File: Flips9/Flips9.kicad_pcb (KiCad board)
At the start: 2 copper layers, 100 x 100 mm, 44 parts, among them CN1 UFP2810, U1 74238, U11 74238, U12 74238, U13 TD62783, U14 ULN2803/2003, U21 74238, U22 74238, U23 TD62783, U24 ULN2803/2003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

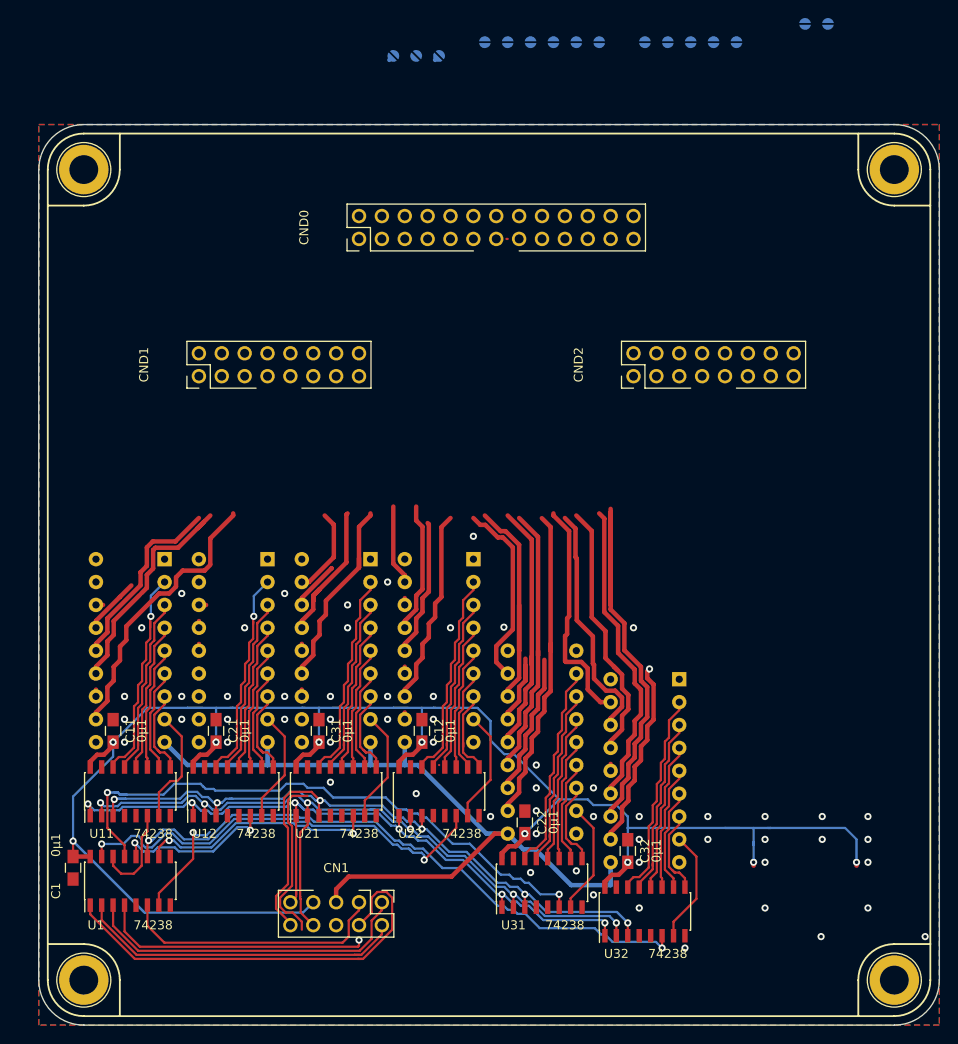
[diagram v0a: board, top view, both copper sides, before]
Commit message: prepare traces of flips9
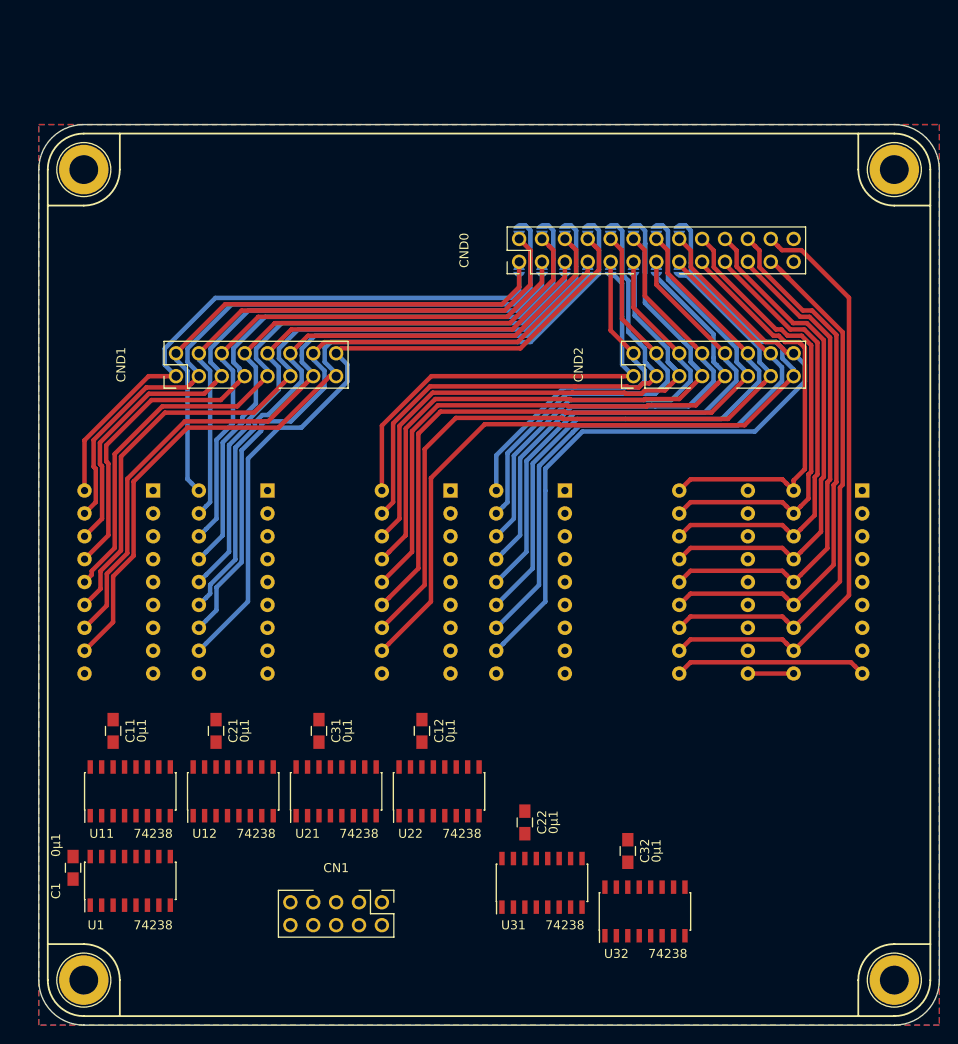
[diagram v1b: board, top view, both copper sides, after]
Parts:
- moved JP115 30.8 mm to (121.9, 67.1), turned to 90 degrees
- moved U34 29.2 mm to (142.2, 91.4)
- moved JP116 28.2 mm to (121.9, 62.5)
- moved JP111 27.9 mm to (116.8, 67.1)
- moved JP101 27.7 mm to (104.1, 67.1), turned to 90 degrees
- moved JP103 26.5 mm to (106.7, 67.1), turned to 90 degrees
- moved JP109 26.2 mm to (114.3, 67.1)
- moved JP113 26.2 mm to (119.4, 67.1)
- moved U33 26.1 mm to (129.5, 91.4)
- moved JP105 25.7 mm to (109.2, 67.1)
- moved JP107 25.7 mm to (111.8, 67.1)
- moved JP110 22.6 mm to (114.3, 62.5), turned to 270 degrees
- moved JP114 22.6 mm to (119.4, 62.5), turned to 270 degrees
- moved JP102 22.4 mm to (104.1, 62.5), turned to 270 degrees
- moved JP104 21.8 mm to (106.7, 62.5), turned to 270 degrees
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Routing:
- net VCC: track 211.6 -> 0.00 mm, vias 9 -> 0
- net /UnitY/A2: track 96.3 -> 0.00 mm, vias 6 -> 0
- net /SX16: track 0.00 -> 89.8 mm
- net /UnitY/A1: track 87.9 -> 0.00 mm, vias 6 -> 0
- net /UnitY/A0: track 84.3 -> 0.00 mm, vias 6 -> 0
- net +24V: track 89.3 -> 5.08 mm
- net /SX7: track 0.76 -> 82.6 mm
- net /SX15: track 0.76 -> 79.6 mm
- net /Y8: track 0.00 -> 78.8 mm
- net /Y16: track 0.76 -> 78.0 mm
- net /SX2: track 0.00 -> 75.8 mm
- net /SX4: track 6.33 -> 81.9 mm
- net /Y7: track 0.00 -> 73.8 mm
- net /Y6: track 0.00 -> 73.4 mm
- net /SX3: track 0.91 -> 72.3 mm
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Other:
- board text removed: "8"
- board text removed: "U34 = ULN2803"

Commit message: Rotate connectors CN1,2
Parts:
- moved CND2 18.0 mm to (134.6, 76.2), turned to 270 degrees
- moved CND1 18.0 mm to (83.8, 76.2), turned to 270 degrees
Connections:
- CND1 pad 1: /SX1 -> /Y8
- CND1 pad 10: /Y5 -> /SX4
- CND1 pad 11: /SX6 -> /Y3
- CND1 pad 12: /Y6 -> /SX3
- CND1 pad 13: /SX7 -> /Y2
- CND1 pad 14: /Y7 -> /SX2
- CND1 pad 15: /SX8 -> /Y1
- CND1 pad 16: /Y8 -> /SX1
- CND1 pad 2: /Y1 -> /SX8
- CND1 pad 3: /SX2 -> /Y7
- CND1 pad 4: /Y2 -> /SX7
- CND1 pad 5: /SX3 -> /Y6
- CND1 pad 6: /Y3 -> /SX6
- CND1 pad 7: /SX4 -> /Y5
- CND1 pad 8: /Y4 -> /SX5
- CND1 pad 9: /SX5 -> /Y4
- CND2 pad 1: /SX9 -> /Y16
- CND2 pad 10: /Y13 -> /SX12
- CND2 pad 11: /SX14 -> /Y11
- CND2 pad 12: /Y14 -> /SX11
- CND2 pad 13: /SX15 -> /Y10
- CND2 pad 14: /Y15 -> /SX10
- CND2 pad 15: /SX16 -> /Y9
- CND2 pad 16: /Y16 -> /SX9
- CND2 pad 2: /Y9 -> /SX16
- CND2 pad 3: /SX10 -> /Y15
- CND2 pad 4: /Y10 -> /SX15
- CND2 pad 5: /SX11 -> /Y14
- CND2 pad 6: /Y11 -> /SX14
- CND2 pad 7: /SX12 -> /Y13
- CND2 pad 8: /Y12 -> /SX13
- CND2 pad 9: /SX13 -> /Y12
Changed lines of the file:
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@@
   (page A4)
   (layers
-    (0 F.Cu signal hide)
+    (0 F.Cu signal)
     (31 B.Cu signal)
     (36 B.SilkS user)
@@
   )
   (module Own:Pin_Header_Straight_Shrouded_Locks_2x08_Pitch2.54mm_ConvNumbering (layer F.Cu)
-    (at 66.04 78.74 90)
+    (at 83.82 76.2 270)
     (descr "Through hole shrouded straight pin header with locks, 2x08, 2.54mm pitch, double rows, conventional numbering")
     (tags "Through hole shrouded straight pin header with locks THT 2x08 2.54mm double row, conventional numbering")
-    (fp_text reference CND1 (at 1.27 -6.096 90) (layer F.SilkS)
-      (effects (font (size 1 1) (thickness 0.15)))
-    )
-    (fp_text value Conn_02x08_Odd_Even (at 4.826 5.08 180) (layer F.Fab) hide
-      (effects (font (size 1 1) (thickness 0.15)))
-    )
-    (fp_text user %R (at 1.27 5.08 180) (layer F.Fab)
+    (fp_text reference CND1 (at 1.27 -6.096 270) (layer F.SilkS)
+      (effects (font (size 1 1) (thickness 0.15)))
+    )
+    (fp_text value Conn_02x08_Odd_Even (at 4.826 5.08) (layer F.Fab) hide
+      (effects (font (size 1 1) (thickness 0.15)))
+    )
+    (fp_text user %R (at 1.27 5.08) (layer F.Fab)
       (effects (font (size 1 1) (thickness 0.15)))
     )
@@
     (fp_line (start -3.33 28.9) (end 5.87 28.9) (layer F.CrtYd) (width 0.05))
     (fp_line (start 5.87 28.9) (end 5.87 -11.12) (layer F.CrtYd) (width 0.05))
-    (pad 1 thru_hole oval (at 0 0 90) (size 1.6 1.6) (drill 1) (layers *.Cu *.Mask)
+    (pad 1 thru_hole oval (at 0 0 270) (size 1.6 1.6) (drill 1) (layers *.Cu *.Mask)
+      (net 74 /Y8))
+    (pad 2 thru_hole oval (at 2.54 0 270) (size 1.6 1.6) (drill 1) (layers *.Cu *.Mask)
+      (net 100 /SX8))
+    (pad 3 thru_hole oval (at 0 2.54 270) (size 1.6 1.6) (drill 1) (layers *.Cu *.Mask)
+      (net 73 /Y7))
+    (pad 4 thru_hole oval (at 2.54 2.54 270) (size 1.6 1.6) (drill 1) (layers *.Cu *.Mask)
+      (net 99 /SX7))
+    (pad 5 thru_hole oval (at 0 5.08 270) (size 1.6 1.6) (drill 1) (layers *.Cu *.Mask)
+      (net 72 /Y6))
+    (pad 6 thru_hole oval (at 2.54 5.08 270) (size 1.6 1.6) (drill 1) (layers *.Cu *.Mask)
+      (net 98 /SX6))
+    (pad 7 thru_hole oval (at 0 7.62 270) (size 1.6 1.6) (drill 1) (layers *.Cu *.Mask)
+      (net 71 /Y5))
+    (pad 8 thru_hole oval (at 2.54 7.62 270) (size 1.6 1.6) (drill 1) (layers *.Cu *.Mask)
+      (net 97 /SX5))
+    (pad 9 thru_hole oval (at 0 10.16 270) (size 1.6 1.6) (drill 1) (layers *.Cu *.Mask)
+      (net 70 /Y4))
+    (pad 10 thru_hole oval (at 2.54 10.16 270) (size 1.6 1.6) (drill 1) (layers *.Cu *.Mask)
+      (net 96 /SX4))
+    (pad 11 thru_hole oval (at 0 12.7 270) (size 1.6 1.6) (drill 1) (layers *.Cu *.Mask)
+      (net 69 /Y3))
+    (pad 12 thru_hole oval (at 2.54 12.7 270) (size 1.6 1.6) (drill 1) (layers *.Cu *.Mask)
+      (net 95 /SX3))
+    (pad 13 thru_hole oval (at 0 15.24 270) (size 1.6 1.6) (drill 1) (layers *.Cu *.Mask)
+      (net 68 /Y2))
+    (pad 14 thru_hole oval (at 2.54 15.24 270) (size 1.6 1.6) (drill 1) (layers *.Cu *.Mask)
+      (net 94 /SX2))
+    (pad 15 thru_hole oval (at 0 17.78 270) (size 1.6 1.6) (drill 1) (layers *.Cu *.Mask)
+      (net 67 /Y1))
+    (pad 16 thru_hole oval (at 2.54 17.78 270) (size 1.6 1.6) (drill 1) (layers *.Cu *.Mask)
       (net 93 /SX1))
-    (pad 2 thru_hole oval (at 2.54 0 90) (size 1.6 1.6) (drill 1) (layers *.Cu *.Mask)
-      (net 67 /Y1))
-    (pad 3 thru_hole oval (at 0 2.54 90) (size 1.6 1.6) (drill 1) (layers *.Cu *.Mask)
-      (net 94 /SX2))
-    (pad 4 thru_hole oval (at 2.54 2.54 90) (size 1.6 1.6) (drill 1) (layers *.Cu *.Mask)
-      (net 68 /Y2))
-    (pad 5 thru_hole oval (at 0 5.08 90) (size 1.6 1.6) (drill 1) (layers *.Cu *.Mask)
-      (net 95 /SX3))
-    (pad 6 thru_hole oval (at 2.54 5.08 90) (size 1.6 1.6) (drill 1) (layers *.Cu *.Mask)
-      (net 69 /Y3))
-    (pad 7 thru_hole oval (at 0 7.62 90) (size 1.6 1.6) (drill 1) (layers *.Cu *.Mask)
-      (net 96 /SX4))
-    (pad 8 thru_hole oval (at 2.54 7.62 90) (size 1.6 1.6) (drill 1) (layers *.Cu *.Mask)
-      (net 70 /Y4))
-    (pad 9 thru_hole oval (at 0 10.16 90) (size 1.6 1.6) (drill 1) (layers *.Cu *.Mask)
-      (net 97 /SX5))
-    (pad 10 thru_hole oval (at 2.54 10.16 90) (size 1.6 1.6) (drill 1) (layers *.Cu *.Mask)
-      (net 71 /Y5))
-    (pad 11 thru_hole oval (at 0 12.7 90) (size 1.6 1.6) (drill 1) (layers *.Cu *.Mask)
-      (net 98 /SX6))
-    (pad 12 thru_hole oval (at 2.54 12.7 90) (size 1.6 1.6) (drill 1) (layers *.Cu *.Mask)
-      (net 72 /Y6))
-    (pad 13 thru_hole oval (at 0 15.24 90) (size 1.6 1.6) (drill 1) (layers *.Cu *.Mask)
-      (net 99 /SX7))
-    (pad 14 thru_hole oval (at 2.54 15.24 90) (size 1.6 1.6) (drill 1) (layers *.Cu *.Mask)
-      (net 73 /Y7))
-    (pad 15 thru_hole oval (at 0 17.78 90) (size 1.6 1.6) (drill 1) (layers *.Cu *.Mask)
-      (net 100 /SX8))
-    (pad 16 thru_hole oval (at 2.54 17.78 90) (size 1.6 1.6) (drill 1) (layers *.Cu *.Mask)
-      (net 74 /Y8))
     (model ${KISYS3DMOD}/Connector_IDC.3dshapes/IDC-Header_2x08_P2.54mm_Vertical.step
       (at (xyz 0 0 0))
@@
   )
   (module Own:Pin_Header_Straight_Shrouded_Locks_2x08_Pitch2.54mm_ConvNumbering (layer F.Cu)
-    (at 116.84 78.74 90)
+    (at 134.62 76.2 270)
     (descr "Through hole shrouded straight pin header with locks, 2x08, 2.54mm pitch, double rows, conventional numbering")
     (tags "Through hole shrouded straight pin header with locks THT 2x08 2.54mm double row, conventional numbering")
-    (fp_text reference CND2 (at 1.27 -6.096 90) (layer F.SilkS)
-      (effects (font (size 1 1) (thickness 0.15)))
-    )
-    (fp_text value Conn_02x08_Odd_Even (at 4.826 5.08 180) (layer F.Fab) hide
+    (fp_text reference CND2 (at 1.27 -6.096 270) (layer F.SilkS)
+      (effects (font (size 1 1) (thickness 0.15)))
+    )
+    (fp_text value Conn_02x08_Odd_Even (at 4.826 5.08) (layer F.Fab) hide
       (effects (font (size 1 1) (thickness 0.15)))
     )
@@
     (fp_line (start -1.33 0) (end -1.33 -1.33) (layer F.SilkS) (width 0.12))
     (fp_line (start -1.33 -1.33) (end 0 -1.33) (layer F.SilkS) (width 0.12))
-    (fp_text user %R (at 1.27 5.08 180) (layer F.Fab)
-      (effects (font (size 1 1) (thickness 0.15)))
-    )
-    (pad 16 thru_hole oval (at 2.54 17.78 90) (size 1.6 1.6) (drill 1) (layers *.Cu *.Mask)
+    (fp_text user %R (at 1.27 5.08) (layer F.Fab)
+      (effects (font (size 1 1) (thickness 0.15)))
+    )
+    (pad 16 thru_hole oval (at 2.54 17.78 270) (size 1.6 1.6) (drill 1) (layers *.Cu *.Mask)
+      (net 108 /SX9))
+    (pad 15 thru_hole oval (at 0 17.78 270) (size 1.6 1.6) (drill 1) (layers *.Cu *.Mask)
+      (net 75 /Y9))
+    (pad 14 thru_hole oval (at 2.54 15.24 270) (size 1.6 1.6) (drill 1) (layers *.Cu *.Mask)
+      (net 107 /SX10))
+    (pad 13 thru_hole oval (at 0 15.24 270) (size 1.6 1.6) (drill 1) (layers *.Cu *.Mask)
+      (net 76 /Y10))
+    (pad 12 thru_hole oval (at 2.54 12.7 270) (size 1.6 1.6) (drill 1) (layers *.Cu *.Mask)
+      (net 106 /SX11))
+    (pad 11 thru_hole oval (at 0 12.7 270) (size 1.6 1.6) (drill 1) (layers *.Cu *.Mask)
+      (net 77 /Y11))
+    (pad 10 thru_hole oval (at 2.54 10.16 270) (size 1.6 1.6) (drill 1) (layers *.Cu *.Mask)
+      (net 105 /SX12))
+    (pad 9 thru_hole oval (at 0 10.16 270) (size 1.6 1.6) (drill 1) (layers *.Cu *.Mask)
+      (net 78 /Y12))
+    (pad 8 thru_hole oval (at 2.54 7.62 270) (size 1.6 1.6) (drill 1) (layers *.Cu *.Mask)
+      (net 104 /SX13))
+    (pad 7 thru_hole oval (at 0 7.62 270) (size 1.6 1.6) (drill 1) (layers *.Cu *.Mask)
+      (net 79 /Y13))
+    (pad 6 thru_hole oval (at 2.54 5.08 270) (size 1.6 1.6) (drill 1) (layers *.Cu *.Mask)
+      (net 103 /SX14))
+    (pad 5 thru_hole oval (at 0 5.08 270) (size 1.6 1.6) (drill 1) (layers *.Cu *.Mask)
+      (net 80 /Y14))
+    (pad 4 thru_hole oval (at 2.54 2.54 270) (size 1.6 1.6) (drill 1) (layers *.Cu *.Mask)
+      (net 102 /SX15))
+    (pad 3 thru_hole oval (at 0 2.54 270) (size 1.6 1.6) (drill 1) (layers *.Cu *.Mask)
+      (net 81 /Y15))
+    (pad 2 thru_hole oval (at 2.54 0 270) (size 1.6 1.6) (drill 1) (layers *.Cu *.Mask)
+      (net 101 /SX16))
+    (pad 1 thru_hole oval (at 0 0 270) (size 1.6 1.6) (drill 1) (layers *.Cu *.Mask)
       (net 82 /Y16))
-    (pad 15 thru_hole oval (at 0 17.78 90) (size 1.6 1.6) (drill 1) (layers *.Cu *.Mask)
-      (net 101 /SX16))
-    (pad 14 thru_hole oval (at 2.54 15.24 90) (size 1.6 1.6) (drill 1) (layers *.Cu *.Mask)
-      (net 81 /Y15))
-    (pad 13 thru_hole oval (at 0 15.24 90) (size 1.6 1.6) (drill 1) (layers *.Cu *.Mask)
-      (net 102 /SX15))
-    (pad 12 thru_hole oval (at 2.54 12.7 90) (size 1.6 1.6) (drill 1) (layers *.Cu *.Mask)
-      (net 80 /Y14))
-    (pad 11 thru_hole oval (at 0 12.7 90) (size 1.6 1.6) (drill 1) (layers *.Cu *.Mask)
-      (net 103 /SX14))
-    (pad 10 thru_hole oval (at 2.54 10.16 90) (size 1.6 1.6) (drill 1) (layers *.Cu *.Mask)
-      (net 79 /Y13))
-    (pad 9 thru_hole oval (at 0 10.16 90) (size 1.6 1.6) (drill 1) (layers *.Cu *.Mask)
-      (net 104 /SX13))
-    (pad 8 thru_hole oval (at 2.54 7.62 90) (size 1.6 1.6) (drill 1) (layers *.Cu *.Mask)
-      (net 78 /Y12))
-    (pad 7 thru_hole oval (at 0 7.62 90) (size 1.6 1.6) (drill 1) (layers *.Cu *.Mask)
-      (net 105 /SX12))
-    (pad 6 thru_hole oval (at 2.54 5.08 90) (size 1.6 1.6) (drill 1) (layers *.Cu *.Mask)
-      (net 77 /Y11))
-    (pad 5 thru_hole oval (at 0 5.08 90) (size 1.6 1.6) (drill 1) (layers *.Cu *.Mask)
-      (net 106 /SX11))
-    (pad 4 thru_hole oval (at 2.54 2.54 90) (size 1.6 1.6) (drill 1) (layers *.Cu *.Mask)
-      (net 76 /Y10))
-    (pad 3 thru_hole oval (at 0 2.54 90) (size 1.6 1.6) (drill 1) (layers *.Cu *.Mask)
-      (net 107 /SX10))
-    (pad 2 thru_hole oval (at 2.54 0 90) (size 1.6 1.6) (drill 1) (layers *.Cu *.Mask)
-      (net 75 /Y9))
-    (pad 1 thru_hole oval (at 0 0 90) (size 1.6 1.6) (drill 1) (layers *.Cu *.Mask)
-      (net 108 /SX9))
     (model ${KISYS3DMOD}/Connector_IDC.3dshapes/IDC-Header_2x08_P2.54mm_Vertical.step
       (at (xyz 0 0 0))

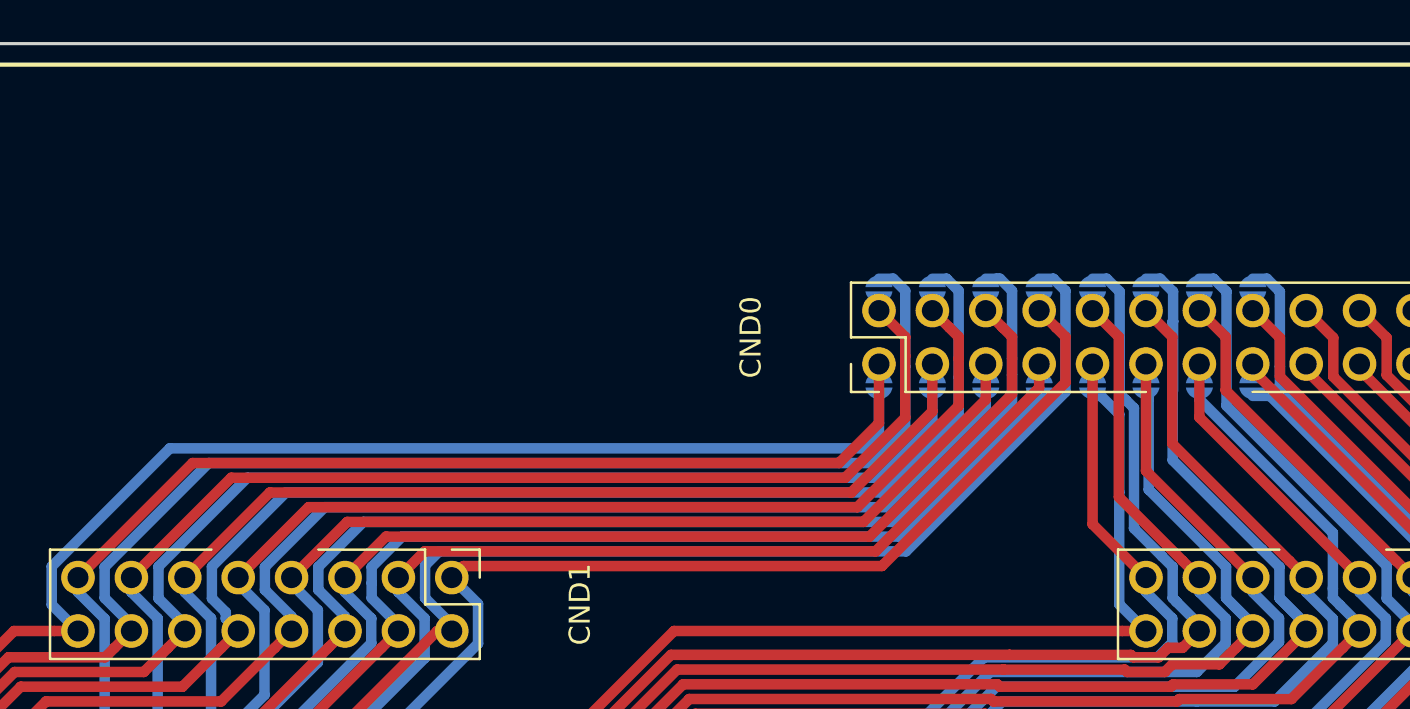
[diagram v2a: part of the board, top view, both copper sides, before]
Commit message: adding extra 16 pin connector instead of reusing 24-pin connector
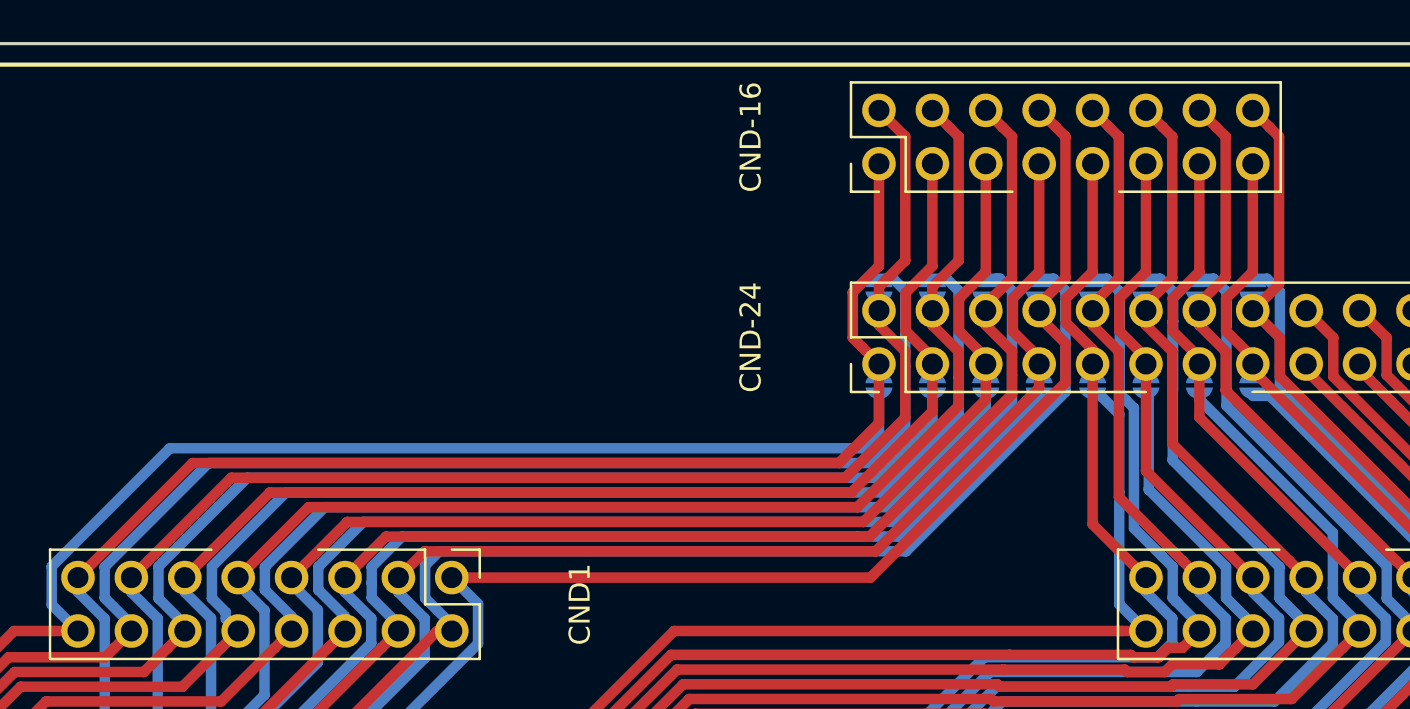
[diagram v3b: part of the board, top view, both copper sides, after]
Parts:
- removed CND0: Conn_02x13_Odd_Even, Own:Pin_Header_Straight_Shrouded_Locks_2x13_Pitch2.54mm_ConvNumbering
- added CND-16: Conn_02x08_Odd_Even, Own:Pin_Header_Straight_Shrouded_Locks_2x08_Pitch2.54mm_ConvNumbering, F.Cu at (104.1, 56.5)
- added CND-24: Conn_02x13_Odd_Even, Own:Pin_Header_Straight_Shrouded_Locks_2x13_Pitch2.54mm_ConvNumbering, F.Cu at (104.1, 66.0)
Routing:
- net /Y3: track 63.5 -> 74.1 mm
- net /Y11: track 48.7 -> 59.3 mm
- net /Y5: track 67.8 -> 78.4 mm
- net /Y15: track 69.0 -> 79.5 mm
- net /Y13: track 58.7 -> 69.3 mm
- net /Y9: track 38.6 -> 49.2 mm
- net /Y7: track 73.8 -> 84.4 mm
- net /Y1: track 60.2 -> 70.8 mm
- net /Y8: track 78.8 -> 89.4 mm
- net /Y6: track 73.4 -> 84.0 mm
- net /Y4: track 68.7 -> 79.3 mm
- net /Y16: track 78.0 -> 88.6 mm
- net /Y14: track 66.9 -> 77.4 mm
- net /Y12: track 56.8 -> 67.4 mm
- net /Y10: track 46.7 -> 57.3 mm
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
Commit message: improve traces
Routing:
- net /SX13: track 69.9 -> 72.8 mm
- net /SX12: track 76.7 -> 74.1 mm
- net /SX14: track 81.4 -> 78.7 mm
- net /SX9: track 49.9 -> 47.4 mm
- net /SX15: track 79.6 -> 77.8 mm
- net /SX11: track 61.9 -> 62.8 mm
